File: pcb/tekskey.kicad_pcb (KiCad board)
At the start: 2 copper layers, 123.8 x 123.8 mm, 83 parts, among them SW0 MX_SW_HS, SW0B1 MX_SW_HS, SW1 MX_SW_HS, SW10 MX_SW_HS, SW11 MX_SW_HS, SW12 MX_SW_HS, SW13 MX_SW_HS, SW14 MX_SW_HS, SW15 MX_SW_HS, SW1B1 MX_SW_HS, SW2 MX_SW_HS, SW20 MX_SW_HS, SW21 MX_SW_HS, SW22 MX_SW_HS, SW23 MX_SW_HS, SW24 MX_SW_HS, SW25 MX_SW_HS, SW2B1 MX_SW_HS, SW3 MX_SW_HS, SW30 MX_SW_HS, SW31 MX_SW_HS, SW32 MX_SW_HS, SW33 MX_SW_HS, SW34 MX_SW_HS, SW35 MX_SW_HS, SW3B1 MX_SW_HS, SW4 MX_SW_HS, SW40 MX_SW_HS, SW41 MX_SW_HS, SW42 MX_SW_HS, SW43 MX_SW_HS, SW44 MX_SW_HS, SW45 MX_SW_HS, SW4B1 MX_SW_HS, SW5 MX_SW_HS, SW50 MX_SW_HS, SW51 MX_SW_HS, SW52 MX_SW_HS, SW53 MX_SW_HS, SW54 MX_SW_HS, SW55 MX_SW_HS

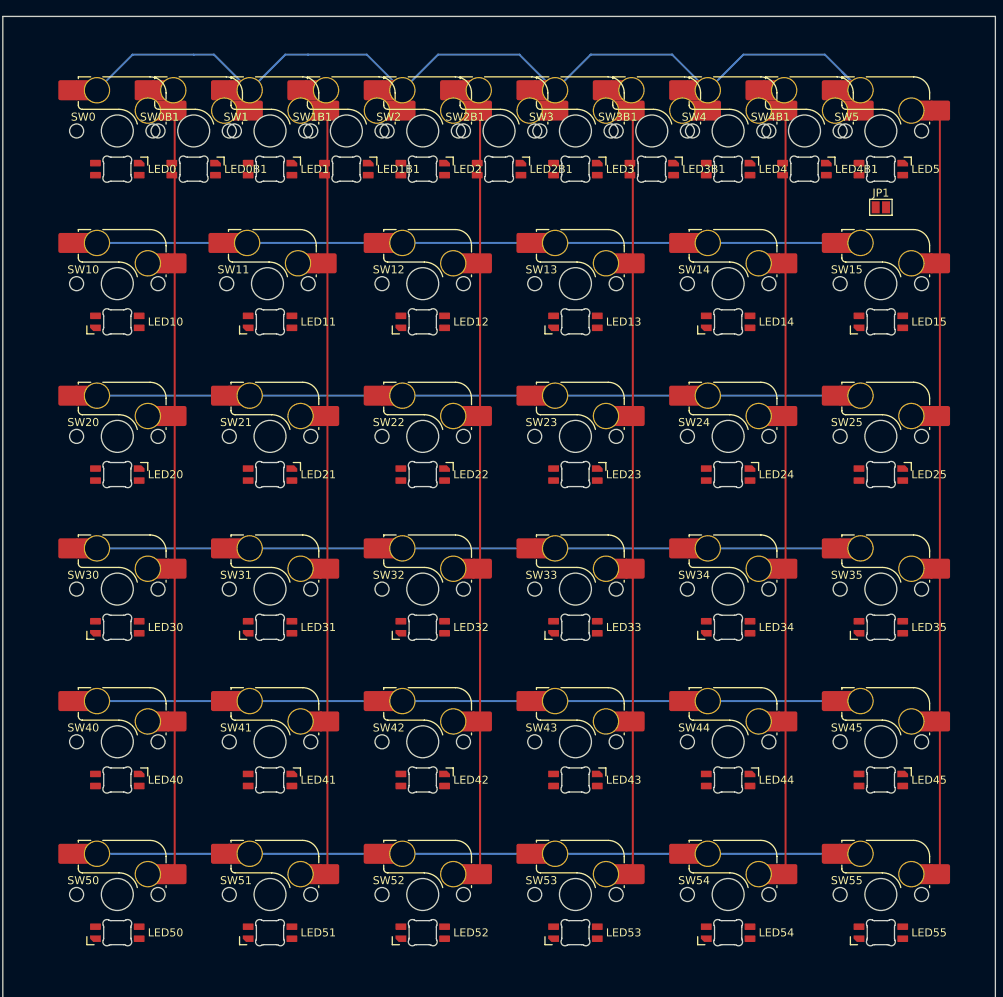
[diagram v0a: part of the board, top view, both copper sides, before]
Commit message: rotate each key
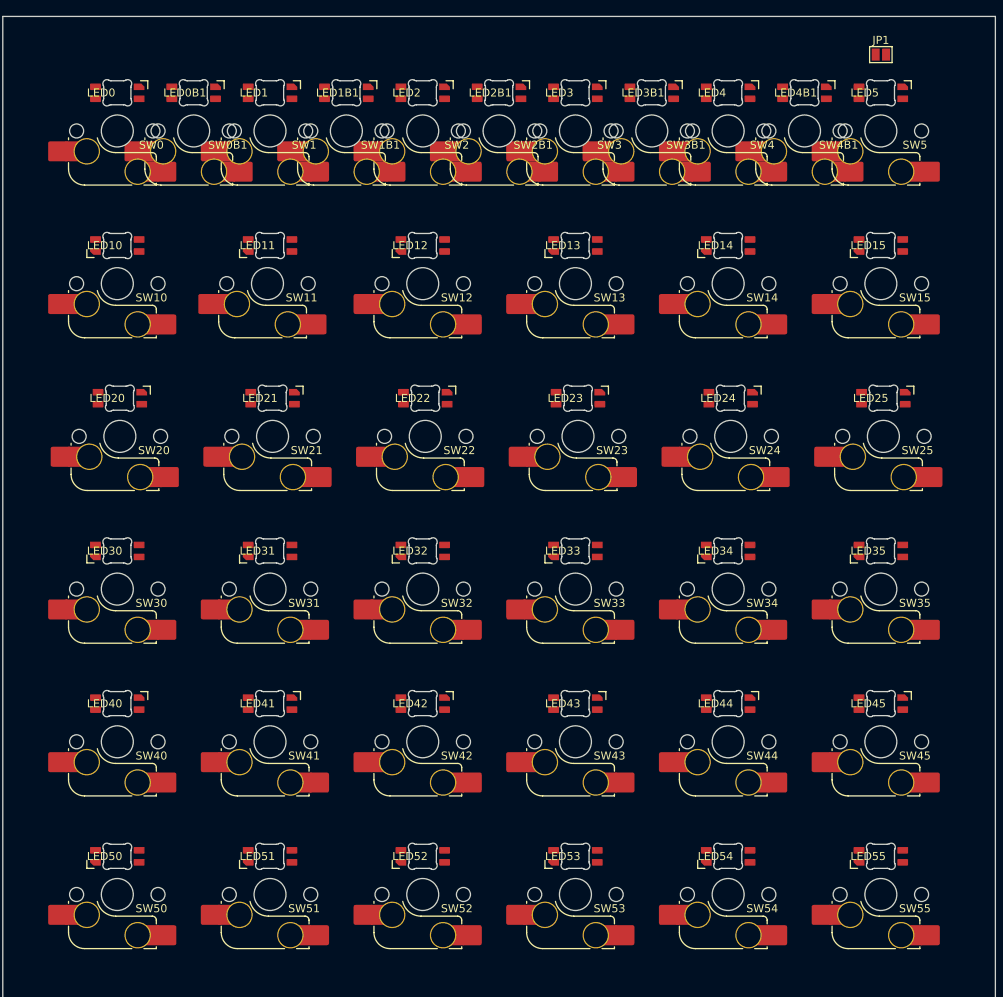
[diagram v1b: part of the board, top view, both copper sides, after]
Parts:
- LED0, LED0B1, LED1, LED1B1, LED2, LED20, LED21, LED22, LED23, LED24, LED25, LED2B1, LED3, LED3B1, LED4, LED40, LED41, LED42, LED43, LED44, LED45, LED4B1, LED5: footprint marbastlib-mx:LED_MX_6028R-FLIPPED -> marbastlib-mx:LED_MX_6028R
- LED10, LED11, LED12, LED13, LED14, LED15, LED30, LED31, LED32, LED33, LED34, LED35, LED50, LED51, LED52, LED53, LED54, LED55: footprint marbastlib-mx:LED_MX_6028R -> marbastlib-mx:LED_MX_6028R-FLIPPED
- moved JP1 19.1 mm to (142.9, 33.3)
- moved LED21 9.53 mm to (67.0, 76.2), turned to 180 degrees
- moved LED22 9.53 mm to (86.0, 76.2), turned to 180 degrees
- moved LED20 9.53 mm to (47.9, 76.2), turned to 180 degrees
- moved LED23 9.53 mm to (105.1, 76.2), turned to 180 degrees
- moved LED24 9.53 mm to (124.1, 76.2), turned to 180 degrees
- moved LED25 9.53 mm to (143.2, 76.2), turned to 180 degrees
- moved LED30 9.53 mm to (47.6, 95.2), turned to 180 degrees
- moved LED31 9.53 mm to (66.7, 95.2), turned to 180 degrees
- moved LED32 9.53 mm to (85.7, 95.2), turned to 180 degrees
- moved LED33 9.53 mm to (104.8, 95.2), turned to 180 degrees
- moved LED34 9.53 mm to (123.8, 95.2), turned to 180 degrees
- moved LED35 9.53 mm to (142.9, 95.2), turned to 180 degrees
- moved LED40 9.53 mm to (47.6, 114.3), turned to 180 degrees
- moved LED41 9.53 mm to (66.7, 114.3), turned to 180 degrees
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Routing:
- net row0: track 118.2 -> 0.00 mm
- net row1: track 96.6 -> 0.00 mm
- net row5: track 95.5 -> 0.00 mm
- net col4: track 95.4 -> 0.00 mm
- net col3: track 95.4 -> 0.00 mm
- net col1: track 95.4 -> 0.00 mm
- net col0: track 95.4 -> 0.00 mm
- net col2: track 95.4 -> 0.00 mm
- net row4: track 95.2 -> 0.00 mm
- net row3: track 95.2 -> 0.00 mm
- net row2: track 95.2 -> 0.00 mm
- net col5: track 95.2 -> 0.00 mm

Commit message: add spacing to f row
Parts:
- moved LED0 4.76 mm to (47.6, 33.3)
- moved LED0B1 4.76 mm to (57.1, 33.3)
- moved LED1 4.76 mm to (66.7, 33.3)
- moved LED1B1 4.76 mm to (76.2, 33.3)
- moved LED2 4.76 mm to (85.7, 33.3)
- moved LED2B1 4.76 mm to (95.2, 33.3)
- moved LED3 4.76 mm to (104.8, 33.3)
- moved LED3B1 4.76 mm to (114.3, 33.3)
- moved LED4 4.76 mm to (123.8, 33.3)
- moved LED4B1 4.76 mm to (133.3, 33.3)
- moved LED5 4.76 mm to (142.9, 33.3)
- moved JP1 4.76 mm to (142.9, 28.6)
- moved SW0 4.76 mm to (47.6, 38.1)
- moved SW0B1 4.76 mm to (57.1, 38.1)
- moved SW1 4.76 mm to (66.7, 38.1)
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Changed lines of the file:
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@@
   )
   (footprint "marbastlib-mx:LED_MX_6028R" (layer "F.Cu")
-    (at 76.2 38.1 180)
+    (at 76.2 33.3375 180)
     (descr "Add-on for regular MX-footprints with 6028 reverse mount LED")
     (tags "cherry MX 6028 rearmount rear mount led rgb backlight")
@@
   )
   (footprint "marbastlib-mx:SW_MX_HS_1u" (layer "F.Cu")
-    (at 57.15 42.8625 180)
+    (at 57.15 38.1 180)
     (descr "Footprint for Cherry MX style switches with Kailh hotswap socket")
     (property "Sheetfile" "tekskey.kicad_sch")
@@
   )
   (footprint "marbastlib-mx:SW_MX_HS_1u" (layer "F.Cu")
-    (at 104.775 42.8625 180)
+    (at 104.775 38.1 180)
     (descr "Footprint for Cherry MX style switches with Kailh hotswap socket")
     (property "Sheetfile" "tekskey.kicad_sch")
@@
   )
   (footprint "marbastlib-mx:SW_MX_HS_1u" (layer "F.Cu")
-    (at 47.625 42.8625 180)
+    (at 47.625 38.1 180)
     (descr "Footprint for Cherry MX style switches with Kailh hotswap socket")
     (property "Sheetfile" "tekskey.kicad_sch")
@@
   )
   (footprint "marbastlib-mx:LED_MX_6028R" (layer "F.Cu")
-    (at 123.825 38.1 180)
+    (at 123.825 33.3375 180)
     (descr "Add-on for regular MX-footprints with 6028 reverse mount LED")
     (tags "cherry MX 6028 rearmount rear mount led rgb backlight")
@@
   )
   (footprint "marbastlib-mx:LED_MX_6028R" (layer "F.Cu")
-    (at 85.725 38.1 180)
+    (at 85.725 33.3375 180)
     (descr "Add-on for regular MX-footprints with 6028 reverse mount LED")
     (tags "cherry MX 6028 rearmount rear mount led rgb backlight")
@@
   )
   (footprint "marbastlib-mx:SW_MX_HS_1u" (layer "F.Cu")
-    (at 85.725 42.8625 180)
+    (at 85.725 38.1 180)
     (descr "Footprint for Cherry MX style switches with Kailh hotswap socket")
     (property "Sheetfile" "tekskey.kicad_sch")
@@
   )
   (footprint "marbastlib-mx:LED_MX_6028R" (layer "F.Cu")
-    (at 47.625 38.1 180)
+    (at 47.625 33.3375 180)
     (descr "Add-on for regular MX-footprints with 6028 reverse mount LED")
     (tags "cherry MX 6028 rearmount rear mount led rgb backlight")
@@
   )
   (footprint "Jumper:SolderJumper-2_P1.3mm_Open_Pad1.0x1.5mm" (layer "F.Cu")
-    (at 142.875 33.3375)
+    (at 142.875 28.575)
     (descr "SMD Solder Jumper, 1x1.5mm Pads, 0.3mm gap, open")
     (tags "solder jumper open")
@@
   )
   (footprint "marbastlib-mx:SW_MX_HS_1u" (layer "F.Cu")
-    (at 114.3 42.8625 180)
+    (at 114.3 38.1 180)
     (descr "Footprint for Cherry MX style switches with Kailh hotswap socket")
     (property "Sheetfile" "tekskey.kicad_sch")
@@
   )
   (footprint "marbastlib-mx:SW_MX_HS_1u" (layer "F.Cu")
-    (at 66.675 42.8625 180)
+    (at 66.675 38.1 180)
     (descr "Footprint for Cherry MX style switches with Kailh hotswap socket")
     (property "Sheetfile" "tekskey.kicad_sch")
@@
   )
   (footprint "marbastlib-mx:LED_MX_6028R" (layer "F.Cu")
-    (at 66.675 38.1 180)
+    (at 66.675 33.3375 180)
     (descr "Add-on for regular MX-footprints with 6028 reverse mount LED")
     (tags "cherry MX 6028 rearmount rear mount led rgb backlight")
@@
   )
   (footprint "marbastlib-mx:SW_MX_HS_1u" (layer "F.Cu")
-    (at 133.35 42.8625 180)
+    (at 133.35 38.1 180)
     (descr "Footprint for Cherry MX style switches with Kailh hotswap socket")
     (property "Sheetfile" "tekskey.kicad_sch")
@@
   )
   (footprint "marbastlib-mx:SW_MX_HS_1u" (layer "F.Cu")
-    (at 142.875 42.8625 180)
+    (at 142.875 38.1 180)
     (descr "Footprint for Cherry MX style switches with Kailh hotswap socket")
     (property "Sheetfile" "tekskey.kicad_sch")
@@
   )
   (footprint "marbastlib-mx:LED_MX_6028R" (layer "F.Cu")
-    (at 114.3 38.1 180)
+    (at 114.3 33.3375 180)
     (descr "Add-on for regular MX-footprints with 6028 reverse mount LED")
     (tags "cherry MX 6028 rearmount rear mount led rgb backlight")
@@
   )
   (footprint "marbastlib-mx:SW_MX_HS_1u" (layer "F.Cu")
-    (at 76.2 42.8625 180)
+    (at 76.2 38.1 180)
     (descr "Footprint for Cherry MX style switches with Kailh hotswap socket")
     (property "Sheetfile" "tekskey.kicad_sch")
@@
   )
   (footprint "marbastlib-mx:LED_MX_6028R" (layer "F.Cu")
-    (at 142.875 38.1 180)
+    (at 142.875 33.3375 180)
     (descr "Add-on for regular MX-footprints with 6028 reverse mount LED")
     (tags "cherry MX 6028 rearmount rear mount led rgb backlight")
@@
   )
   (footprint "marbastlib-mx:SW_MX_HS_1u" (layer "F.Cu")
-    (at 123.825 42.8625 180)
+    (at 123.825 38.1 180)
     (descr "Footprint for Cherry MX style switches with Kailh hotswap socket")
     (property "Sheetfile" "tekskey.kicad_sch")
@@
   )
   (footprint "marbastlib-mx:LED_MX_6028R" (layer "F.Cu")
-    (at 57.15 38.1 180)
+    (at 57.15 33.3375 180)
     (descr "Add-on for regular MX-footprints with 6028 reverse mount LED")
     (tags "cherry MX 6028 rearmount rear mount led rgb backlight")
@@
   )
   (footprint "marbastlib-mx:LED_MX_6028R" (layer "F.Cu")
-    (at 104.775 38.1 180)
+    (at 104.775 33.3375 180)
     (descr "Add-on for regular MX-footprints with 6028 reverse mount LED")
     (tags "cherry MX 6028 rearmount rear mount led rgb backlight")
@@
   )
   (footprint "marbastlib-mx:LED_MX_6028R" (layer "F.Cu")
-    (at 95.25 38.1 180)
+    (at 95.25 33.3375 180)
     (descr "Add-on for regular MX-footprints with 6028 reverse mount LED")
     (tags "cherry MX 6028 rearmount rear mount led rgb backlight")
@@
   )
   (footprint "marbastlib-mx:LED_MX_6028R" (layer "F.Cu")
-    (at 133.35 38.1 180)
+    (at 133.35 33.3375 180)
     (descr "Add-on for regular MX-footprints with 6028 reverse mount LED")
     (tags "cherry MX 6028 rearmount rear mount led rgb backlight")
@@
   )
   (footprint "marbastlib-mx:SW_MX_HS_1u" (layer "F.Cu")
-    (at 95.25 42.8625 180)
+    (at 95.25 38.1 180)
     (descr "Footprint for Cherry MX style switches with Kailh hotswap socket")
     (property "Sheetfile" "tekskey.kicad_sch")
@@
     )
   )
-  (gr_rect (start 33.3375 28.575) (end 157.1625 152.4) (layer "Edge.Cuts") (width 0.1) (fill none))
+  (gr_rect (start 33.3375 23.8125) (end 157.1625 147.6375) (layer "Edge.Cuts") (width 0.1) (fill none))
 )

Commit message: add led jumper
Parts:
- removed SW0B1: MX_SW_HS, marbastlib-mx:SW_MX_HS_1u
- added JP10: Jumper_2_Open, Jumper:SolderJumper-2_P1.3mm_Open_Pad1.0x1.5mm, F.Cu at (123.8, 28.6)
- added JP11: Jumper_2_Open, Jumper:SolderJumper-2_P1.3mm_Open_Pad1.0x1.5mm, F.Cu at (133.3, 28.6)
- added JP12: Jumper_2_Open, Jumper:SolderJumper-2_P1.3mm_Open_Pad1.0x1.5mm, F.Cu at (47.6, 128.6)
- added JP13: Jumper_2_Open, Jumper:SolderJumper-2_P1.3mm_Open_Pad1.0x1.5mm, F.Cu at (57.1, 128.6)
- added JP14: Jumper_2_Open, Jumper:SolderJumper-2_P1.3mm_Open_Pad1.0x1.5mm, F.Cu at (66.7, 128.6)
- added JP15: Jumper_2_Open, Jumper:SolderJumper-2_P1.3mm_Open_Pad1.0x1.5mm, F.Cu at (123.8, 128.6)
- added JP16: Jumper_2_Open, Jumper:SolderJumper-2_P1.3mm_Open_Pad1.0x1.5mm, F.Cu at (133.3, 128.6)
- added JP17: Jumper_2_Open, Jumper:SolderJumper-2_P1.3mm_Open_Pad1.0x1.5mm, F.Cu at (142.9, 128.6)
- added JP2: Jumper_2_Open, Jumper:SolderJumper-2_P1.3mm_Open_Pad1.0x1.5mm, F.Cu at (47.6, 28.6)
- added JP3: Jumper_2_Open, Jumper:SolderJumper-2_P1.3mm_Open_Pad1.0x1.5mm, F.Cu at (57.1, 28.6)
- added JP4: Jumper_2_Open, Jumper:SolderJumper-2_P1.3mm_Open_Pad1.0x1.5mm, F.Cu at (66.7, 28.6)
- added JP5: Jumper_2_Open, Jumper:SolderJumper-2_P1.3mm_Open_Pad1.0x1.5mm, F.Cu at (76.2, 28.6)
- added JP6: Jumper_2_Open, Jumper:SolderJumper-2_P1.3mm_Open_Pad1.0x1.5mm, F.Cu at (85.7, 28.6)
- added JP7: Jumper_2_Open, Jumper:SolderJumper-2_P1.3mm_Open_Pad1.0x1.5mm, F.Cu at (94.6, 28.6)
- added JP8: Jumper_2_Open, Jumper:SolderJumper-2_P1.3mm_Open_Pad1.0x1.5mm, F.Cu at (104.8, 28.6)
- added JP9: Jumper_2_Open, Jumper:SolderJumper-2_P1.3mm_Open_Pad1.0x1.5mm, F.Cu at (114.3, 28.6)
- added LED6: MX_SK6812MINI-E, marbastlib-mx:LED_MX_6028R-FLIPPED, F.Cu at (57.1, 133.3)
- added LED7: MX_SK6812MINI-E, marbastlib-mx:LED_MX_6028R-FLIPPED, F.Cu at (133.3, 133.3)
- added SW51B1: MX_SW_HS, marbastlib-mx:SW_MX_HS_1u, F.Cu at (57.1, 138.1)
- added SW55B1: MX_SW_HS, marbastlib-mx:SW_MX_HS_1u, F.Cu at (133.3, 138.1)
- added SW5B1: MX_SW_HS, marbastlib-mx:SW_MX_HS_1u, F.Cu at (133.3, 38.1)
- moved SW1B1 19.1 mm to (57.1, 38.1)
- moved SW2B1 19.0 mm to (76.2, 38.1)
- moved SW3B1 19.0 mm to (95.2, 38.1)
- moved SW4B1 19.0 mm to (114.3, 38.1)
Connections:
- JP1 pad 1: Net-(LED4-Pad3) -> Net-(JP1-Pad1)
- LED0B1 pad 2: Net-(LED10-Pad3) -> Net-(LED0-Pad3)
- LED0B1 pad 3: Net-(LED0-Pad3) -> Net-(LED0B1-Pad3)
- LED1 pad 2: Net-(LED0-Pad3) -> Net-(LED0B1-Pad3)
- LED1 pad 3: Net-(LED1B1-Pad3) -> Net-(LED1B1-Pad2)
- LED1B1 pad 2: Net-(LED0-Pad3) -> Net-(LED1B1-Pad2)
- LED1B1 pad 3: Net-(LED1B1-Pad3) -> Net-(LED2-Pad2)
- LED2 pad 2: Net-(LED1B1-Pad3) -> Net-(LED2-Pad2)
- LED2 pad 3: Net-(LED2B1-Pad3) -> Net-(LED2-Pad3)
- LED2B1 pad 2: Net-(LED1B1-Pad3) -> Net-(LED2-Pad3)
- LED3B1 pad 2: Net-(LED2B1-Pad3) -> Net-(LED3-Pad3)
- LED3B1 pad 3: Net-(LED3-Pad3) -> Net-(LED3B1-Pad3)
- LED4 pad 2: Net-(LED3-Pad3) -> Net-(LED3B1-Pad3)
- LED4B1 pad 2: Net-(LED3-Pad3) -> Net-(LED4-Pad3)
- LED4B1 pad 3: Net-(LED4-Pad3) -> Net-(JP1-Pad1)
- LED5 pad 2: Net-(LED4-Pad3) -> Net-(JP1-Pad1)
- LED51 pad 3: Net-(LED50-Pad2) -> Net-(LED51-Pad3)
- LED55 pad 3: Net-(LED54-Pad2) -> Net-(LED55-Pad3)

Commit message: remove some jumpers
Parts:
- removed JP12, JP13, JP14, JP15, JP16, JP17: Jumper_2_Open, Jumper:SolderJumper-2_P1.3mm_Open_Pad1.0x1.5mm
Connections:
- LED50 pad 2: Net-(LED50-Pad2) -> Net-(LED51-Pad3)
- LED53 pad 2: Net-(LED53-Pad2) -> Net-(LED7-Pad3)
- LED54 pad 2: Net-(LED54-Pad2) -> Net-(LED55-Pad3)
- LED54 pad 3: Net-(LED53-Pad2) -> Net-(LED7-Pad3)
- LED6 pad 2: Net-(LED51-Pad3) -> Net-(LED51-Pad2)
- LED6 pad 3: Net-(LED50-Pad2) -> Net-(LED40-Pad2)
- LED7 pad 2: Net-(LED55-Pad3) -> LEDOUT
- LED7 pad 3: Net-(LED54-Pad2) -> Net-(LED7-Pad3)
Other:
- board size 123.8 x 123.8 mm -> 123.8 x 128.6 mm
